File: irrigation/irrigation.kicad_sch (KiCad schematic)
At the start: 46 parts, among them J1 24V Jmp, J10 24V, J11 25%, J12 50%, J13 75%, J14 100%, J15 100%, J16 100%, J17 Pump, J18 Outlet Pump, J19 Empty, J2 Power, J20 25%, J21 25%, J3 Power, J4 Power, J5 Power, J6 Power, J7 Power, J8 0V Jmp, J9 Empty, K1 PLC-RPT-24DC/21, K2 PLC-RPT-24DC/21, K3 PLC-RPT-24DC/21, K4 PLC-RPT-24DC/21, M1 Well Pump, M2 Outlet Pump, SW1 Well Empty, SW2 100% Full, SW3 25% Full, SW4 50% Full, SW5 75% Full, SW6 Drain Switch, SW7 Fill Switch, U1 MPPT-Charger

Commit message: Layout
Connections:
- net at J10.: now also J15.; no longer J14.
- net at J16.: now also J15.; no longer J14.
- net at J21.: now also J11.; no longer J20.
- net at J20.: now also K4.A1
- new net: J10., J14.
- new net: J14., J16.
- new net: J20., J21.
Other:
- moved on the sheet: D2, D6, J18, J19, J9, K1, K3, M2, SW1, SW6, SW7

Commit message: More numbers
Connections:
- net Empty LEV Out is gone; now on net Empty LED Out: J7.
- net at J10.: now also J15.; no longer J14.
- net at J16.: now also J15.; no longer J14.
- net at J21.: now also J11.; no longer J20.
- net at J20.: now also K4.A1
- new net: J10., J14.
- new net: J14., J16.
- new net: J20., J21.

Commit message: Finished updates
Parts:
- removed J19: Empty, symbol Phoenix Contact:PTTB_2,5-L/N_3210994
- added J22, J23: PT 6-TWIN, symbol Phoenix Contact:PT 6-TWIN
- added K5: PLC-RPT-24DC/21, symbol Phoenix Contact:PLC-RPT-24DC/21
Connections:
- net MPPT Load - is gone; now on net Power: J6.
- net 4: now also J23.; no longer BT2.2 (-)
- net 5: now also J22.; no longer BT1.1 (+)
- net Drain Switch 0V: now also K3.A2
- net Drain Switch 24V: now also SW6.1 (A)
- net Load +: now also U1.5 (Load+), K5.A1; no longer CB1.
- net Load -: now also K5.A2
- net at J10.: now also J15.; no longer J14.
- net at J16.: now also J15.; no longer J14.
- net 40: now reaches K3.11, K4.14
- net 42: now reaches J18., K3.14
- net 39: now reaches K3.A1, SW6.2 (B)
- net 47: now reaches J18., M2.1 (+)
- net 48: now reaches J18., M2.2 (-)
- net at J21.: now also J11.; no longer J20.
- net 49: now reaches K1.A1, SW7.2 (B)
- net 41: now reaches J20.
- net 41: now also K4.A1
- net 2 renamed Batt +
- net Batt +: now also K5.11; no longer U1.5 (Load+)
- net MPPT Load + renamed Power
- net Power: now also K5.14
- new net: J10., J14.
- new net: J14., J16.
- new net: BT2.2 (-), J23.
- new net: BT1.1 (+), J22.
- new net: J20., J21.
- new net 3: CB1., J22.
- new net Batt -: J23., J6.
- no-connect marks 30 -> 33
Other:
- note added: "Load Control"
- moved on the sheet: BT1, BT2, CB1, D1, D2, D3, D4, D5, D6, J10, J11, J12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

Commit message: paper size
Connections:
- net at J10.: now also J15.; no longer J14.
- net at J16.: now also J15.; no longer J14.
- net at J21.: now also J11.; no longer J20.
- new net: J10., J14.
- new net: J14., J16.
- new net: J20., J21.
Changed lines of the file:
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@@
 	(generator "eeschema")
 	(generator_version "9.0")
-	(paper "B")
+	(paper "USLedger")
 	(title_block
 		(title "Irrigation Phase 1")

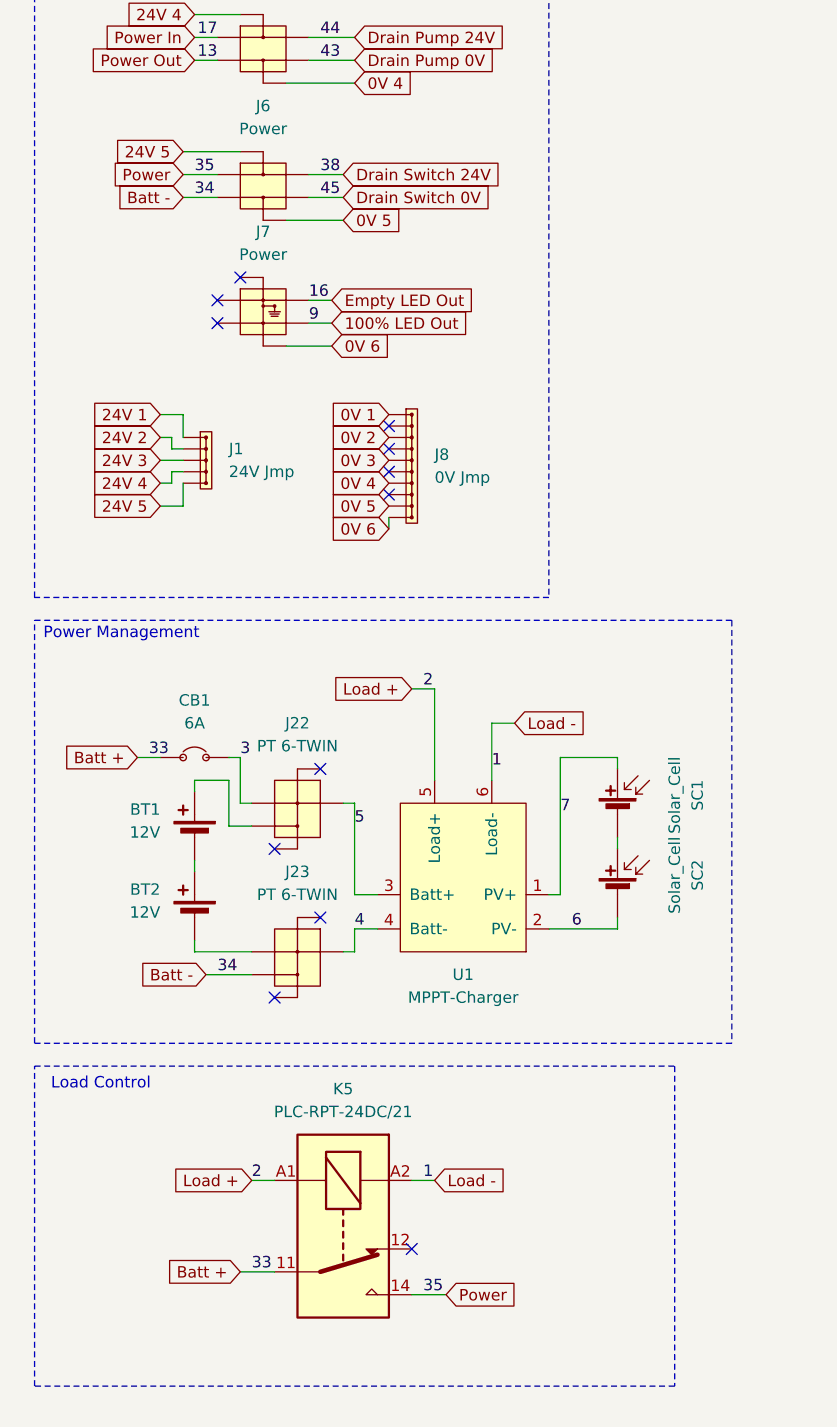
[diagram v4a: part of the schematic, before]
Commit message: Updating after deleting load relay
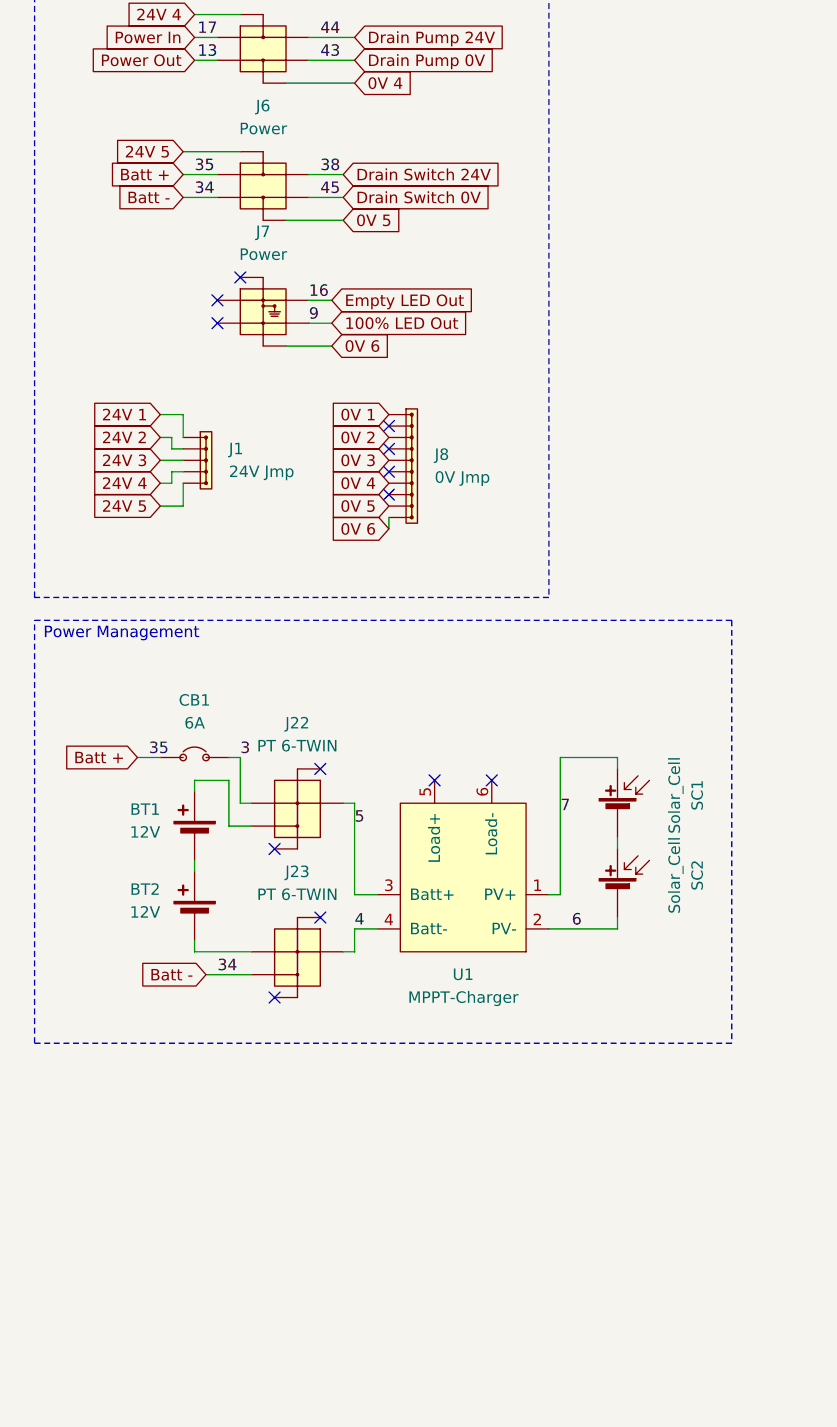
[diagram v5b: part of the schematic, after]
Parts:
- removed K5: PLC-RPT-24DC/21, symbol Phoenix Contact:PLC-RPT-24DC/21
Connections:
- net Power is gone; now on net Drain Switch 24V: J6.
- net Batt +: now also J6.
- net at J10.: now also J15.; no longer J14.
- net at J16.: now also J15.; no longer J14.
- net at J21.: now also J11.; no longer J20.
- net Load +: no longer names the net of U1.5 (Load+)
- net Load -: no longer names the net of U1.6 (Load-)
- new net: J10., J14.
- new net: J14., J16.
- new net: J20., J21.
- no-connect marks 33 -> 34
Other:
- note removed: "Load Control"

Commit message: Cleanup for readme
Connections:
- net at J10.: now also J15.; no longer J14.
- net at J16.: now also J15.; no longer J14.
- net at J21.: now also J11.; no longer J20.
- new net: J10., J14.
- new net: J14., J16.
- new net: J20., J21.
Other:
- moved on the sheet: D1, D2, D3, D4, D5, D6, K1, K2, SW6

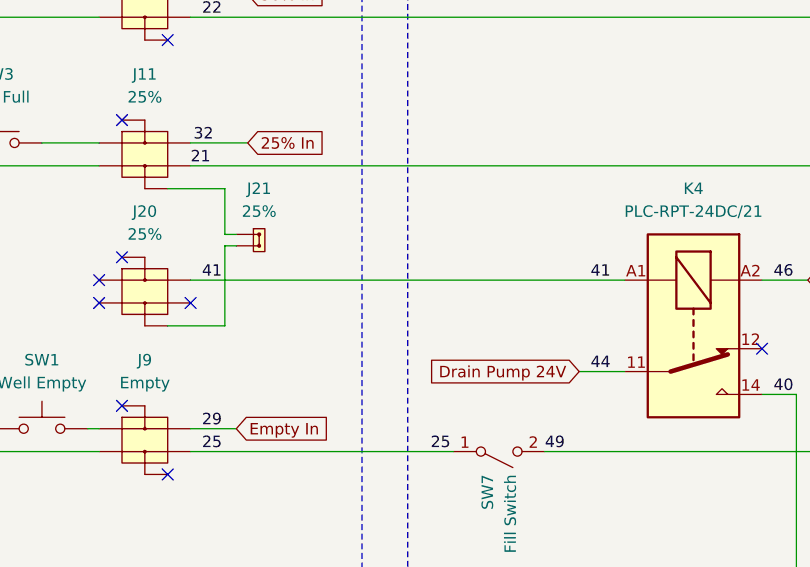
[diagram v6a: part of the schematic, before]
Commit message: Fixing the drain relay input
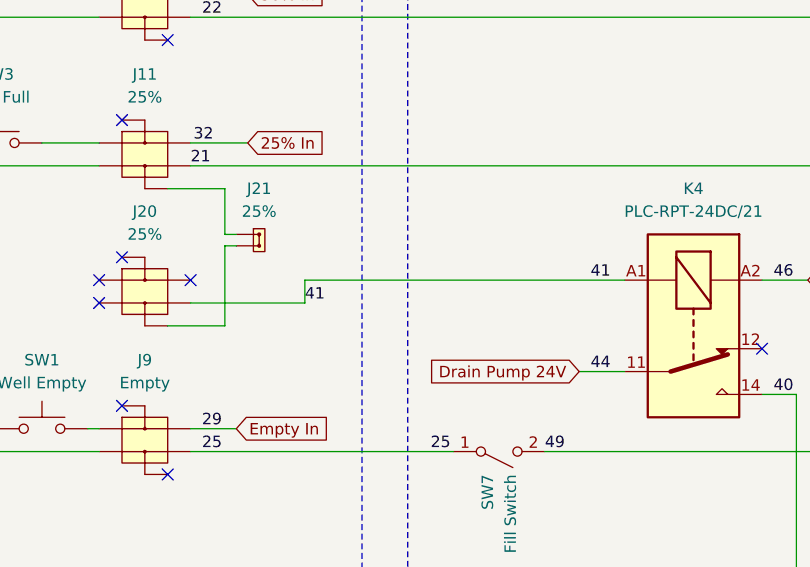
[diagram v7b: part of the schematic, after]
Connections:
- net at J10.: now also J15.; no longer J14.
- net at J16.: now also J15.; no longer J14.
- net at J21.: now also J11.; no longer J20.
- new net: J10., J14.
- new net: J14., J16.
- new net: J20., J21.
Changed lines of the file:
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@@
+	)
+	(no_connect
+		(at 139.7 127)
 	)
 	(no_connect
@@
 	)
 	(no_connect
-		(at 139.7 129.54)
-	)
-	(no_connect
 		(at 46.99 154.94)
 	)
@@
 	(wire
 		(pts
+			(xy 152.4 127) (xy 187.96 127)
+		)
+		(stroke
+			(width 0)
+			(type default)
+		)
+	)
+	(wire
+		(pts
 			(xy 128.27 27.94) (xy 127 27.94)
 		)
@@
 	(wire
 		(pts
-			(xy 139.7 127) (xy 187.96 127)
-		)
-		(stroke
-			(width 0)
-			(type default)
-		)
-	)
-	(wire
-		(pts
 			(xy 128.27 33.02) (xy 113.03 33.02)
 		)
@@
 	(wire
 		(pts
+			(xy 139.7 129.54) (xy 152.4 129.54)
+		)
+		(stroke
+			(width 0)
+			(type default)
+		)
+	)
+	(wire
+		(pts
 			(xy 111.76 111.76) (xy 113.03 111.76)
 		)
@@
 		(pts
 			(xy 129.54 81.28) (xy 116.84 81.28)
+		)
+		(stroke
+			(width 0)
+			(type default)
+		)
+	)
+	(wire
+		(pts
+			(xy 152.4 129.54) (xy 152.4 127)
 		)
 		(stroke
@@
 	)
 	(label "41"
-		(at 140.97 127 0)
-		(effects
-			(font
+		(at 152.4 129.54 0)
+		(effects
+			(font

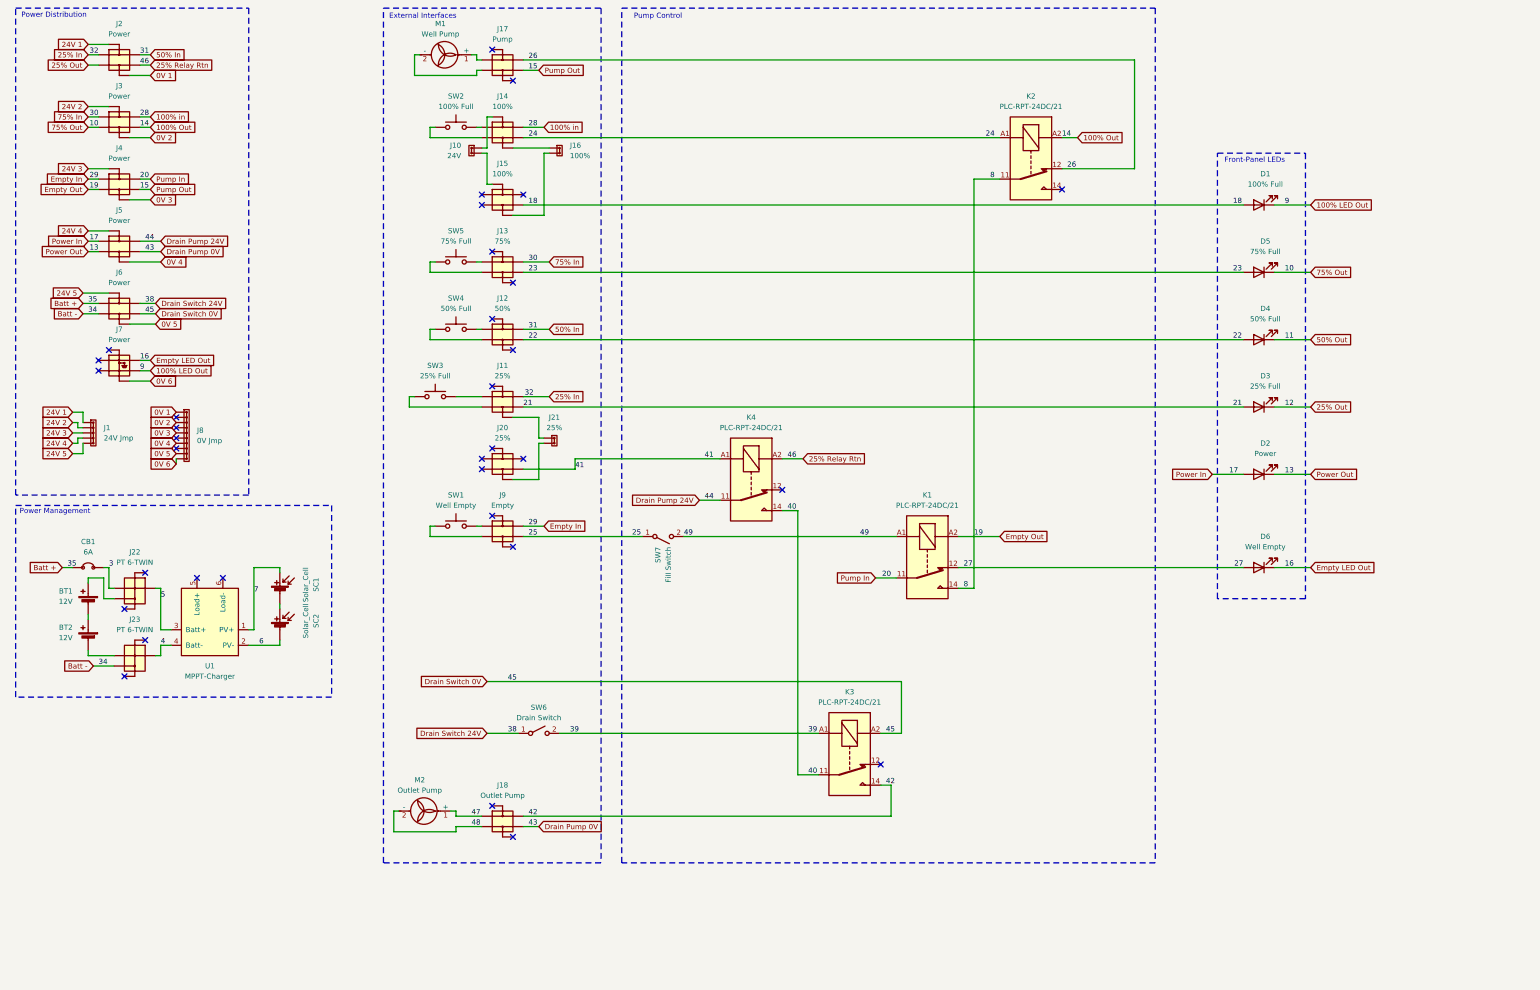
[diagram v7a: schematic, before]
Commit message: Couple more fixes
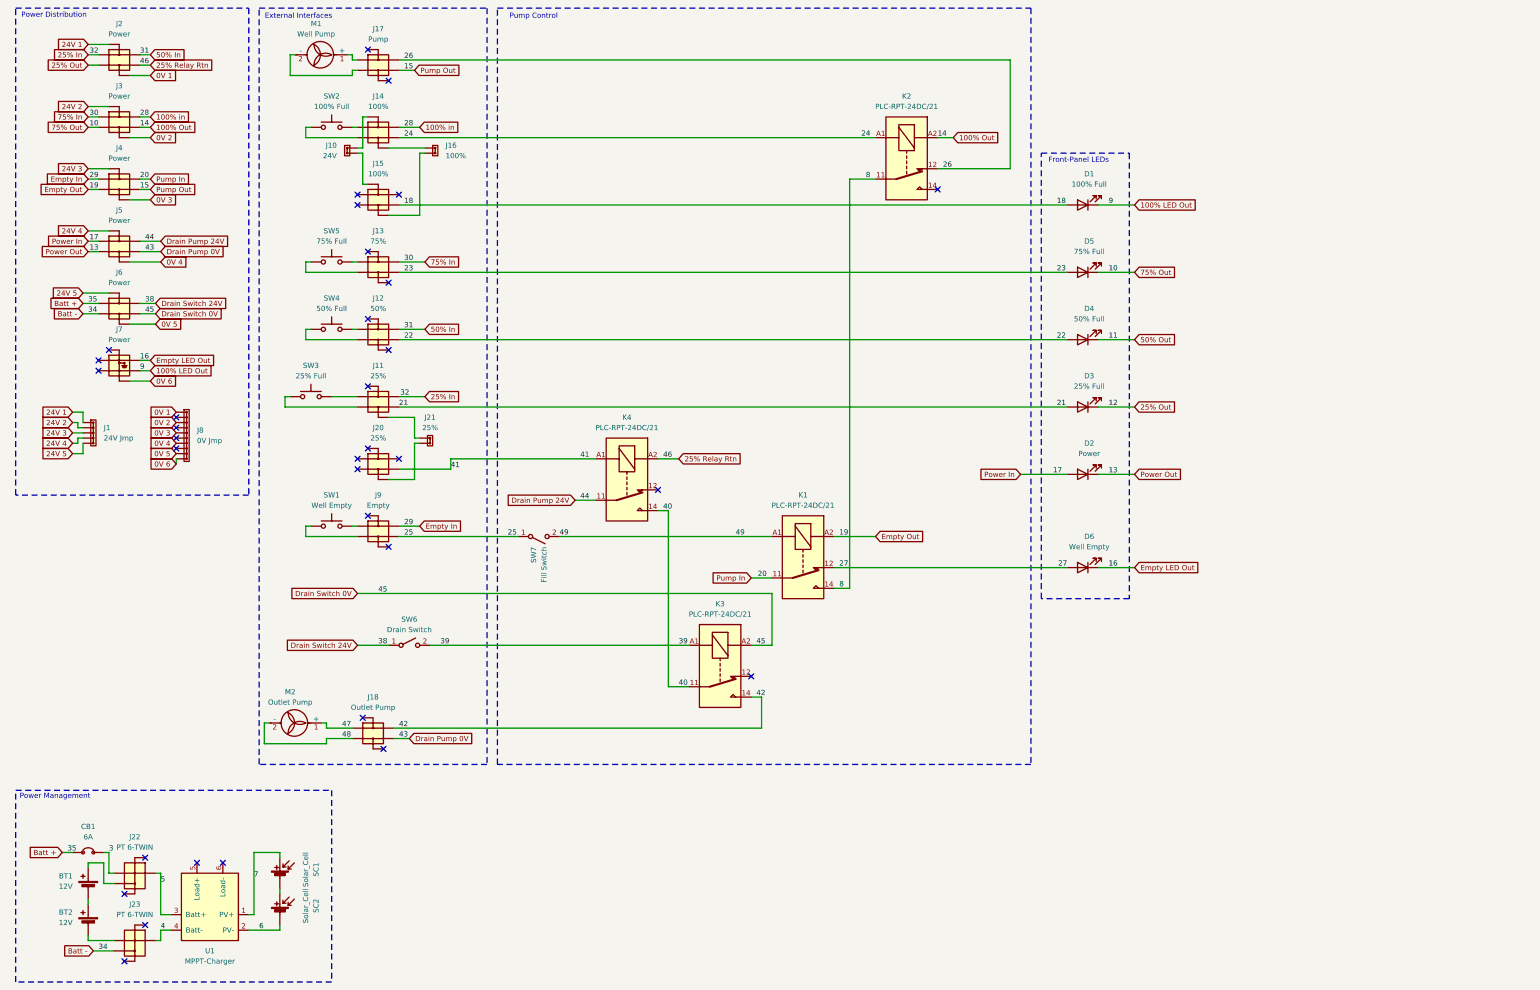
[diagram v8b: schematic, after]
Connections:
- net Empty Out: no longer K1.14, K2.11
- net at J10.: now also J15.; no longer J14.
- net at J16.: now also J15.; no longer J14.
- net at J21.: now also J11.; no longer J20.
- new net: J10., J14.
- new net: J14., J16.
- new net: J20., J21.
- new net 8: K1.14, K2.11
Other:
- moved on the sheet: BT1, BT2, CB1, D1, D2, D3, D4, D5, D6, J10, J11, J12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
